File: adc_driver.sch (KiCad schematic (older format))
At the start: 25 parts, among them U17 DG412xUE, U18 AD8421ARZ, U19 ADA4932-1YCPZ-R7

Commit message: made sheet for Howland
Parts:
- removed U19: ADA4932-1YCPZ-R7, digikey-footprints:VFQFN-16-1EP_3x3mm, symbol covg-kicad:ADA4932-1YCPZ-R7
- added U24: LMP8350MA_NOPB, covg-kicad:LMP8350MA&slash_NOPB, symbol covg-kicad:LMP8350MA_NOPB
- U22: renamed from U?; footprint PW16_TEX -> Package_SO:TSSOP-16_4.4x5mm_P0.65mm
- gave numbers to parts that had none: 4
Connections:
- wire segments 107 -> 104
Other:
- moved on the sheet: C14, C16, C17, C18, R39, R40, R41, R42, R43, R44, R45, R58

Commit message: layout updates; part positioning
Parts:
- U22: Manf# (none) -> TMUX6136PWR
- U24: footprint covg-kicad:LMP8350MA&slash_NOPB -> Package_SO:SOIC-8_3.9x4.9mm_P1.27mm; Manf# (none) -> LMP8350MA/NOPB
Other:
- note added: "4.7 uF for the AD8421 inamp"
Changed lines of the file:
@@
 F 2 "Package_SO:TSSOP-16_4.4x5mm_P0.65mm" H 3800 1550 60  0001 C CNN
 F 3 "" H 3150 1450 60  0000 C CNN
+F 4 "TMUX6136PWR" H 3150 1450 50  0001 C CNN "Manf#"
 	1    3150 1450
 	1    0    0    -1
@@
 F 0 "U24" H 7950 3750 60  0000 C CNN
 F 1 "LMP8350MA_NOPB" H 8300 3650 60  0000 C CNN
-F 2 "covg-kicad:LMP8350MA&slash_NOPB" H 8200 3750 60  0001 C CNN
+F 2 "Package_SO:SOIC-8_3.9x4.9mm_P1.27mm" H 8200 3750 60  0001 C CNN
 F 3 "" H 7700 3650 60  0000 C CNN
+F 4 "LMP8350MA/NOPB" H 7700 3650 50  0001 C CNN "Manf#"
 	1    7700 3650
 	1    0    0    -1
@@
 Wire Bus Line
 	900  3450 3050 3450
+Text Notes 4800 6800 0    50   ~ 0
+4.7 uF for the AD8421 inamp
 $EndSCHEMATC

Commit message: layout updates and 3d models
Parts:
- U18: footprint digikey-footprints:TSSOP-8_W3mm -> Package_SO:TSSOP-8_3x3mm_P0.65mm
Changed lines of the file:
@@
 $Descr A4 11693 8268
 encoding utf-8
-Sheet 6 7
+Sheet 5 7
 Title ""
 Date ""
@@
 F 0 "U18" H 5694 3796 50  0000 L CNN
 F 1 "AD8421ARZ" H 5694 3705 50  0000 L CNN
-F 2 "digikey-footprints:TSSOP-8_W3mm" H 5050 3750 50  0001 C CNN
+F 2 "Package_SO:TSSOP-8_3x3mm_P0.65mm" H 5050 3750 50  0001 C CNN
 F 3 "https://www.analog.com/media/en/technical-documentation/data-sheets/AD8421.pdf" H 5600 3350 50  0001 C CNN
 F 4 "AD8421ARMZ" H 5694 3896 50  0001 C CNN "Manf#"

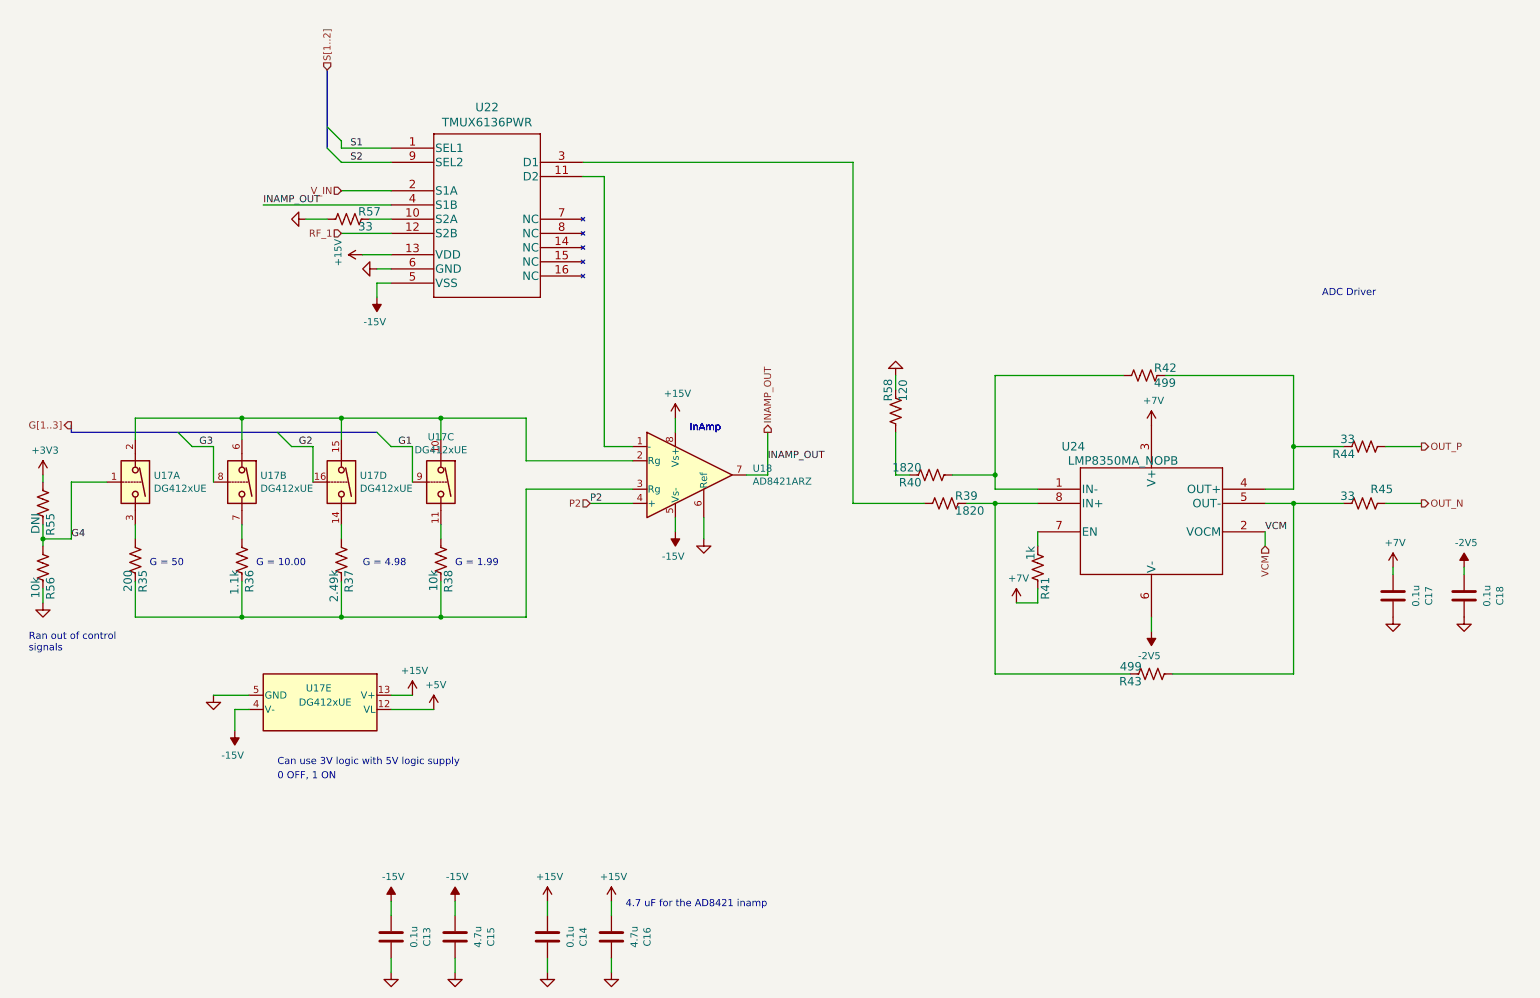
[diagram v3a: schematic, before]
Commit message: updates to README
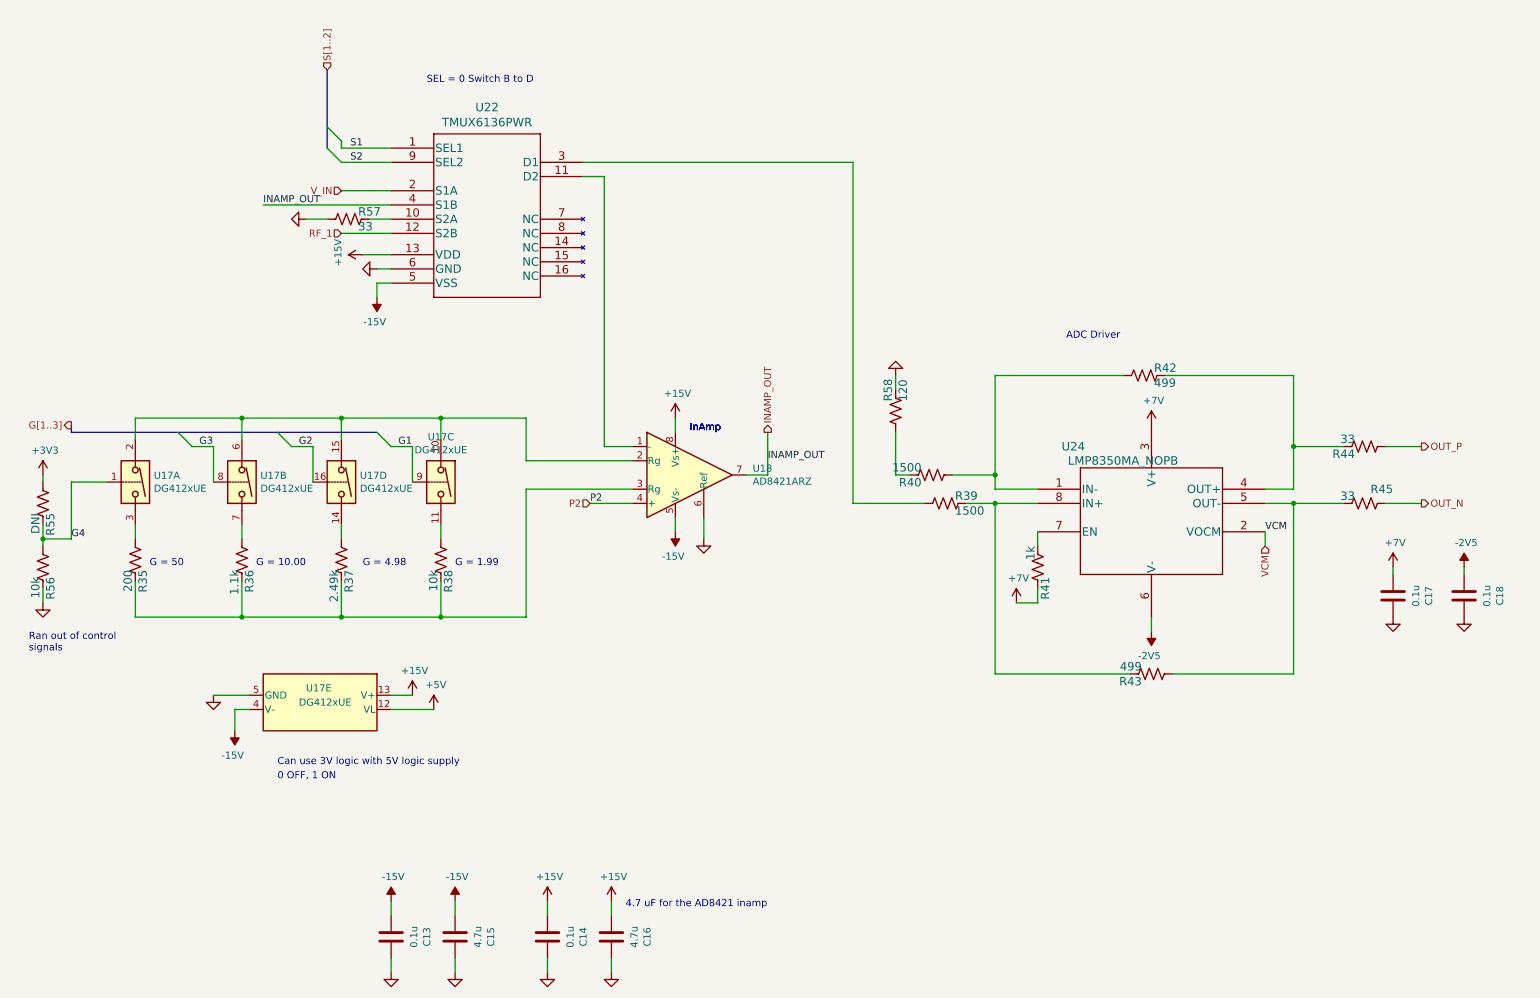
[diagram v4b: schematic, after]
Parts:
- R39, R40: value 1820 -> 1500; Manf# RC0603FR-071K82L -> RC0603FR-071K5L
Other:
- note added: "ADC Driver \nUsing alternative part LMP8350\nWas ADA4932 (but supply issues)"
- note added: "SEL = 0 Switch B to D\n SEL = 1 Switch A to D"
- note removed: "ADC Driver \nAlternative part LMP8350"
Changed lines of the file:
@@
 AR Path="/6032F251/608FDC40/6097B98D" Ref="R39"  Part="1"
 F 0 "R39" V 6997 4018 59  0000 L CNN
-F 1 "1820" V 7102 4018 59  0000 L CNN
+F 1 "1500" V 7102 4018 59  0000 L CNN
 F 2 "Resistor_SMD:R_0603_1608Metric" H 7050 3950 50  0001 C CNN
 F 3 "" H 7050 3950 50  0001 C CNN
-F 4 "RC0603FR-071K82L" H 6997 4118 50  0001 C CNN "Manf#"
+F 4 "RC0603FR-071K5L" H 6997 4118 50  0001 C CNN "Manf#"
 F 5 "1%" H 7050 3950 50  0001 C CNN "Tolerance"
 	1    7050 3950
@@
 AR Path="/6032F251/608FDC40/6097B99B" Ref="R40"  Part="1"
 F 0 "R40" V 6897 3818 59  0000 L CNN
-F 1 "1820" V 7002 3818 59  0000 L CNN
+F 1 "1500" V 7002 3818 59  0000 L CNN
 F 2 "Resistor_SMD:R_0603_1608Metric" H 6950 3750 50  0001 C CNN
 F 3 "" H 6950 3750 50  0001 C CNN
-F 4 "RC0603FR-071K82L" H 6897 3918 50  0001 C CNN "Manf#"
+F 4 "RC0603FR-071K5L" H 6897 3918 50  0001 C CNN "Manf#"
 F 5 "1%" H 6950 3750 50  0001 C CNN "Tolerance"
 	1    6950 3750
@@
 Text Label 9300 4150 0    50   ~ 0
 VCM
-Text Notes 9700 2500 0    50   ~ 0
-ADC Driver \nAlternative part LMP8350
+Text Notes 7900 2800 0    50   ~ 0
+ADC Driver \nUsing alternative part LMP8350\nWas ADA4932 (but supply issues)
 Text HLabel 4550 3950 0    50   Input ~ 0
 P2
@@
 Wire Wire Line
 	2800 1450 2800 1400
+Text Notes 4800 6800 0    50   ~ 0
+4.7 uF for the AD8421 inamp
 Wire Bus Line
 	2700 900  2700 1450
 Wire Bus Line
 	900  3450 3050 3450
-Text Notes 4800 6800 0    50   ~ 0
-4.7 uF for the AD8421 inamp
+Text Notes 3400 1000 0    50   ~ 0
+SEL = 0 Switch B to D\n SEL = 1 Switch A to D
 $EndSCHEMATC

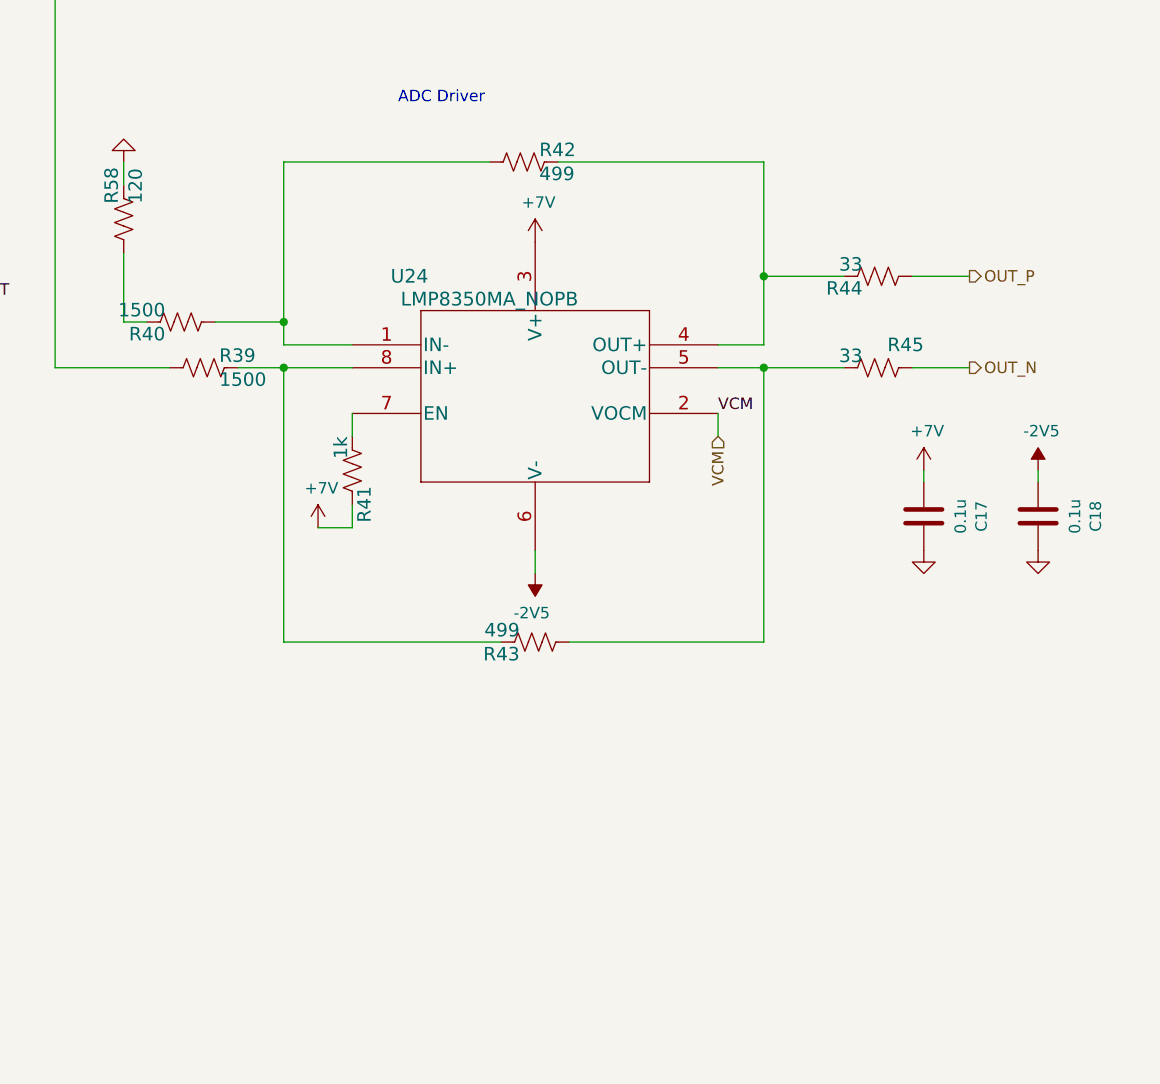
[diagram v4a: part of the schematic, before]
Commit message: updates to schematic plot
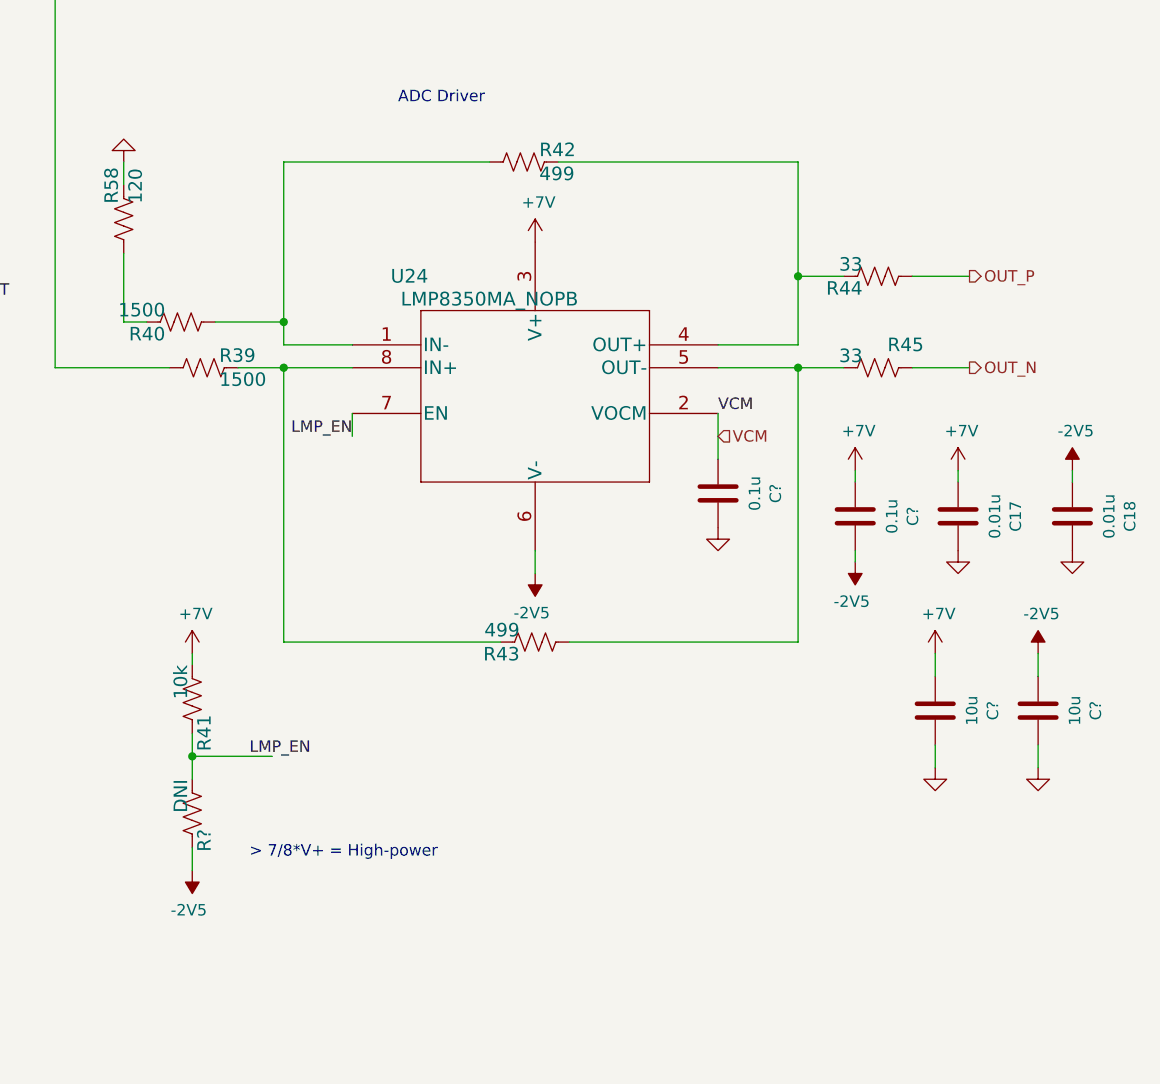
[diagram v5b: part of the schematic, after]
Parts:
- added C? (x2): 10u, Capacitor_SMD:C_1206_3216Metric, symbol Device:C
- added C? (x2): 0.1u, Capacitor_SMD:C_0603_1608Metric, symbol Device:C
- added R?: DNI, Resistor_SMD:R_0603_1608Metric, symbol Device:R_US
- C17, C18: value 0.1u -> 0.01u; Manf# CC0603MRX7R8BB104 -> CC0603MRX7R8BB103
- R41: value 1k -> 10k; Manf# RC0603FR-071KL -> RC0603FR-0710KL
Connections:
- net +7V: now also R41.2, C?.2, C?.2; no longer R41.1
- net -2V5: now also C?.1, C?.2, R?.1
- net GND: now also C?.1, C?.1, C?.1
- net VCM: now also C?.2
- net LMP_EN: now reaches U24.7 (EN)
- net LMP_EN: now also R41.1, R?.2; no longer R41.2
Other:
- note added: "> 7/8*V+ = High-power\n >5/8*V+ = Mid-power\n>3/8*V+ = low-power\n"
- moved on the sheet: C17, C18, R41
